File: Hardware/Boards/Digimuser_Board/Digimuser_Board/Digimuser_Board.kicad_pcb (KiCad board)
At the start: 2 copper layers, 60.2 x 38.7 mm, 74 parts, among them J1 Conn_01x01, J10 Conn_01x01, J11 Conn_01x01, J12 Conn_01x01, J13 Conn_01x01, J14 Conn_01x01, J15 Conn_01x01, J2 Conn_01x01, J3 Barrel_Jack_MountingPin, J4 Conn_01x03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

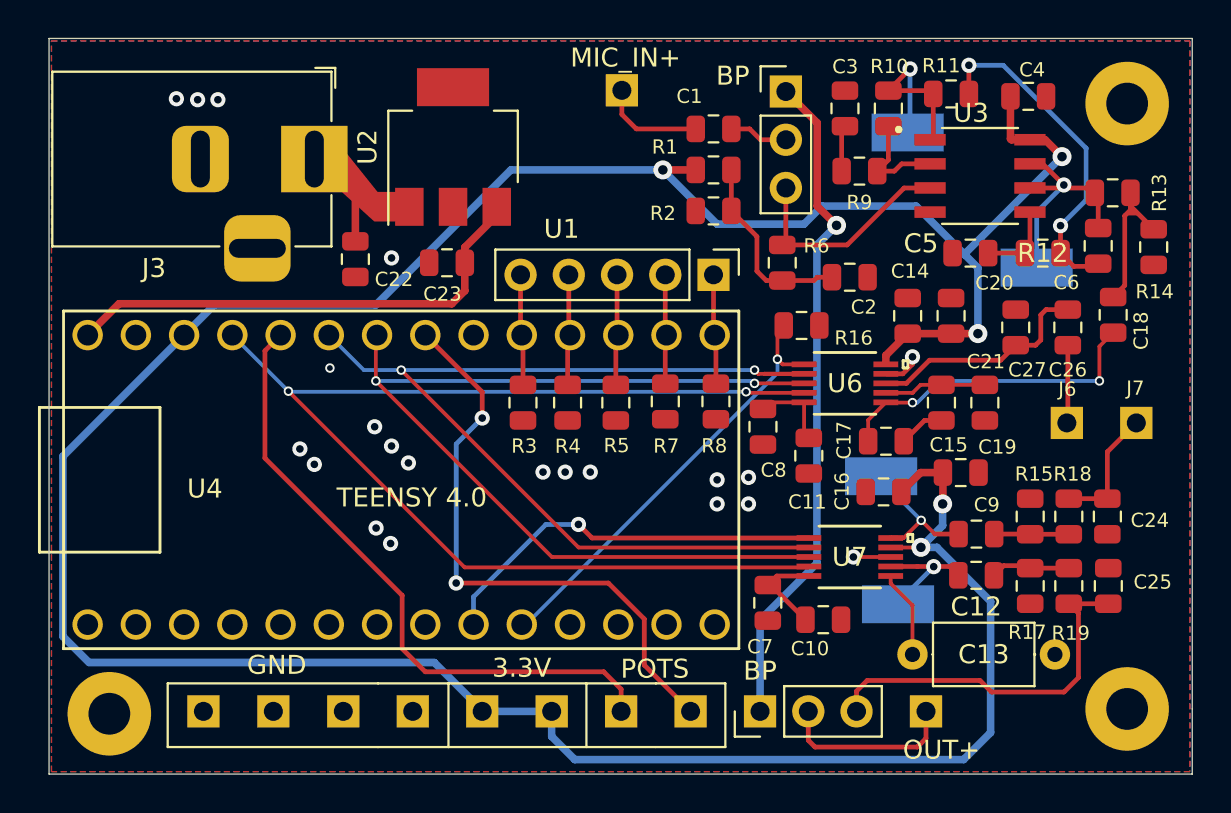
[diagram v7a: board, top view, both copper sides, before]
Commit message: Sent board out for review. Received feedback and made changes to the PCB layout accordingly. Changes include: Pin headers spaced 0.1in, Labeling Teensy connection pins, updating voltage regulator GNDing. Board sent for a second review. Currently on RevA1 for DIGIMUSER.
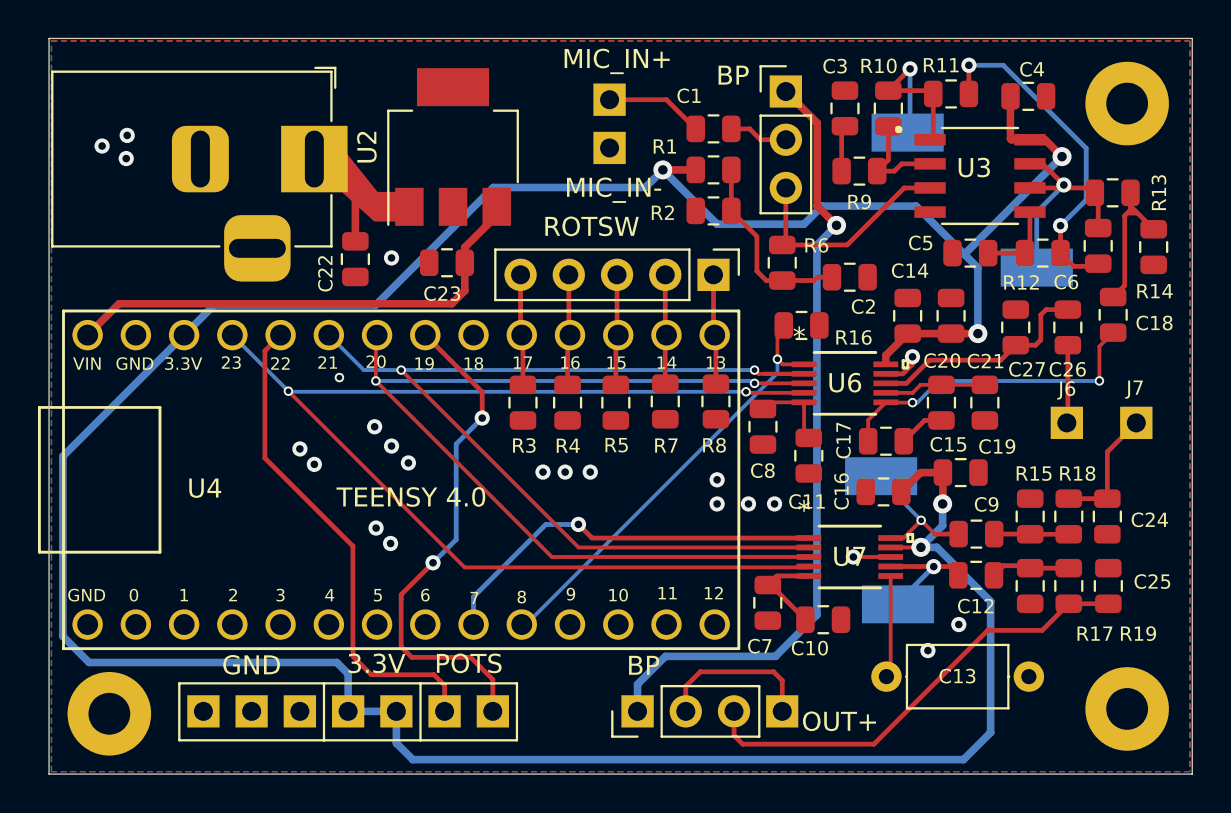
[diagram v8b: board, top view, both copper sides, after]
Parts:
- U2: footprint Package_TO_SOT_SMD:SOT-223 -> Package_TO_SOT_SMD:SOT-223-3_TabPin2
- U6: value CS5343-CZZ -> CIR-TSSOP-10
- U7: value CS4344-CZZ -> CIR-TSSOP-10
- moved J2 34.5 mm to (131.1, 72.4)
- moved J15 10.4 mm to (125.0, 102.1)
- moved J9 9.30 mm to (122.4, 102.1)
- moved J13 8.18 mm to (119.9, 102.1)
- moved J11 7.57 mm to (140.2, 102.1)
- moved J8 7.06 mm to (117.3, 102.1)
- moved J5 6.45 mm to (132.6, 102.1)
- moved J14 5.94 mm to (114.8, 102.1)
- moved J12 4.83 mm to (112.3, 102.1)
- moved C13 1.80 mm to (145.7, 100.3)
- moved J1 0.82 mm to (131.1, 69.9)
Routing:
- net Net-(J9-Pad1): track 33.4 -> 26.0 mm
- net BYPASS: track 35.4 -> 41.5 mm
- net Net-(J15-Pad1): track 31.4 -> 26.6 mm
- net Net-(C25-Pad1): track 19.7 -> 24.2 mm
- net 3.3V: track 163.4 -> 164.7 mm
- net Net-(J11-Pad1): track 9.48 -> 8.53 mm
- net Net-(C13-Pad1): track 4.51 -> 5.39 mm
- net GND: vias 21 -> 23
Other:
- board text added: "0"
- board text added: "1"
- board text added: "10"
- board text added: "11"
- board text added: "12"
- board text added: "13"
- board text added: "14"
- board text added: "15"
- board text added: "16"
- board text added: "17"
- board text added: "18"
- board text added: "19"
- board text added: "2"
- board text added: "20"
- board text added: "21"
- board text added: "22"
- board text added: "23"
- board text added: "3"
- board text added: "4"
- board text added: "5"
- board text added: "6"
- board text added: "7"
- board text added: "8"
- board text added: "9"
- board text added: "DIGIMUSER REV. A DESIGNER: DAVID WALKER-HOWELL"
- board text added: "MIC_IN-"
- board text added: "ROTSW"
- board text added: "VIN"
